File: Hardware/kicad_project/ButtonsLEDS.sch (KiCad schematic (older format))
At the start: 100 parts

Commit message: update project with corrected schematic / pcb
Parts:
- removed C? (x25): 1u, RandomJunk:C_0402_NoSilk, symbol Device:C
- removed D? (x25): D, RandomJunk:D_SOD-323F_less_silk, symbol Device:D
- removed D? (x25): WS2812B, RandomJunk:ws2812b-2020-lightpipe, symbol customLibrary:WS2812B-2020
- removed SW? (x25): spst_4_pin_internal, RandomJunk:ts1102_smallerpads_buttonhole, symbol customLibrary:spst_4_pin_internal
- added C10, C11, C12, C13, C14, C15, C16, C17, C18, C19, C20, C21, C22, C23, C24, C25, C6, C7, C8, C9: 1u, Capacitors_SMD:C_0402_NoSilk, symbol Device:C
- added D10, D11, D12, D13, D14, D15, D16, D17, D18, D19, D20, D21, D22, D23, D24, D25, D6, D7, D8, D9: WS2812B, RandomJunk:ws2812b-2020-lightpipe, symbol customLibrary:WS2812B-2020
- added D26, D27, D28, D29, D30, D31, D32, D33, D34, D35, D36, D37, D38, D39, D40, D41, D42, D43, D44, D45, D46, D47, D48, D49, D50: D, RandomJunk:D_SOD-323F_less_silk, symbol Device:D
- added SW1, SW10, SW11, SW12, SW13, SW14, SW15, SW16, SW17, SW18, SW19, SW2, SW20, SW21, SW22, SW23, SW24, SW25, SW3, SW4, SW5, SW6, SW7, SW8, SW9: spst_4_pin_internal, RandomJunk:ts1102_smallerpads_buttonhole, symbol customLibrary:spst_4_pin_internal
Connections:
- net +3V3: now also C10.1, C11.1, C12.1, C13.1, C14.1, C15.1, C16.1, C17.1, C18.1, C19.1, C20.1, C21.1, C22.1, C23.1, C24.1, C25.1, C6.1, C7.1, C8.1, C9.1, D10.4 (VDD), D11.4 (VDD), D12.4 (VDD), D13.4 (VDD), D14.4 (VDD), D15.4 (VDD), D16.4 (VDD), D17.4 (VDD), D18.4 (VDD), D19.4 (VDD), D20.4 (VDD), D21.4 (VDD), D22.4 (VDD), D23.4 (VDD), D24.4 (VDD), D25.4 (VDD), D6.4 (VDD), D7.4 (VDD), D8.4 (VDD), D9.4 (VDD)
- net GND: now also C10.2, C11.2, C12.2, C13.2, C14.2, C15.2, C16.2, C17.2, C18.2, C19.2, C20.2, C21.2, C22.2, C23.2, C24.2, C25.2, C6.2, C7.2, C8.2, C9.2, D10.2 (VSS), D11.2 (VSS), D12.2 (VSS), D13.2 (VSS), D14.2 (VSS), D15.2 (VSS), D16.2 (VSS), D17.2 (VSS), D18.2 (VSS), D19.2 (VSS), D20.2 (VSS), D21.2 (VSS), D22.2 (VSS), D23.2 (VSS), D24.2 (VSS), D25.2 (VSS), D6.2 (VSS), D7.2 (VSS), D8.2 (VSS), D9.2 (VSS)
- net key_col1: now also SW1.4
- net key_col2: now also SW2.4
- net key_col3: now also SW3.4
- net key_col4: now also SW4.4
- net key_col5: now also SW5.4
- net key_row1: now also D26.1 (K), D27.1 (K), D28.1 (K), D29.1 (K), D30.1 (K)
- net key_row2: now also D31.1 (K), D32.1 (K), D33.1 (K), D34.1 (K), D35.1 (K)
- net key_row3: now also D36.1 (K), D37.1 (K), D38.1 (K), D39.1 (K), D40.1 (K)
- net key_row4: now also D41.1 (K), D42.1 (K), D43.1 (K), D44.1 (K), D45.1 (K)
- net key_row5: now also D46.1 (K), D47.1 (K), D48.1 (K), D49.1 (K), D50.1 (K)
- net led_din: now also D6.3 (DIN)
- new net: D50.2 (A), SW25.1
- new net: SW20.3, SW25.4
- new net: D49.2 (A), SW24.1
- new net: SW19.3, SW24.4
- new net: D48.2 (A), SW23.1
- new net: SW18.3, SW23.4
- new net: D47.2 (A), SW22.1
- new net: SW17.3, SW22.4
- new net: D46.2 (A), SW21.1
- new net: SW16.3, SW21.4
- new net: D45.2 (A), SW20.1
- new net: SW15.3, SW20.4
- new net: D44.2 (A), SW19.1
- new net: SW14.3, SW19.4
- new net: D43.2 (A), SW18.1
- new net: SW13.3, SW18.4
- new net: D42.2 (A), SW17.1
- new net: SW12.3, SW17.4
- new net: D41.2 (A), SW16.1
- new net: SW11.3, SW16.4
- new net: D40.2 (A), SW15.1
- new net: SW10.3, SW15.4
- new net: D39.2 (A), SW14.1
- new net: SW14.4, SW9.3
- new net: D38.2 (A), SW13.1
- new net: SW13.4, SW8.3
- new net: D37.2 (A), SW12.1
- new net: SW12.4, SW7.3
- new net: D36.2 (A), SW11.1
- new net: SW11.4, SW6.3
- new net: D35.2 (A), SW10.1
- new net: SW10.4, SW5.3
- new net: D34.2 (A), SW9.1
- new net: SW4.3, SW9.4
- new net: D33.2 (A), SW8.1
- new net: SW3.3, SW8.4
- new net: D32.2 (A), SW7.1
- new net: SW2.3, SW7.4
- new net: D31.2 (A), SW6.1
- new net: SW1.3, SW6.4
- new net: D30.2 (A), SW5.1
- new net: D29.2 (A), SW4.1
- new net: D28.2 (A), SW3.1
- new net: D27.2 (A), SW2.1
- new net: D26.2 (A), SW1.1
- new net: D24.1 (DOUT), D25.3 (DIN)
- new net: D23.1 (DOUT), D24.3 (DIN)
- new net: D22.1 (DOUT), D23.3 (DIN)
- new net: D21.1 (DOUT), D22.3 (DIN)
- new net: D20.1 (DOUT), D21.3 (DIN)
- new net: D19.1 (DOUT), D20.3 (DIN)
- new net: D18.1 (DOUT), D19.3 (DIN)
- new net: D17.1 (DOUT), D18.3 (DIN)
- new net: D16.1 (DOUT), D17.3 (DIN)
- new net: D15.1 (DOUT), D16.3 (DIN)
- new net: D14.1 (DOUT), D15.3 (DIN)
- new net: D13.1 (DOUT), D14.3 (DIN)
- new net: D12.1 (DOUT), D13.3 (DIN)
- new net: D11.1 (DOUT), D12.3 (DIN)
- new net: D10.1 (DOUT), D11.3 (DIN)
- new net: D10.3 (DIN), D9.1 (DOUT)
- new net: D8.1 (DOUT), D9.3 (DIN)
- new net: D7.1 (DOUT), D8.3 (DIN)
- new net: D6.1 (DOUT), D7.3 (DIN)

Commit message: initial firmware commit, update hardware
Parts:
- D10, D11, D12, D13, D14, D15, D16, D17, D18, D19, D20, D21, D22, D23, D24, D25, D6, D7, D8, D9: LCSC C965555 -> C965556
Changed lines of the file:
@@
 F 2 "RandomJunk:ws2812b-2020-lightpipe" H 5150 5300 50  0001 L TNN
 F 3 "https://cdn-shop.adafruit.com/datasheets/WS2812B.pdf" H 5200 5225 50  0001 L TNN
-F 4 "C965555" H 5100 5600 50  0001 C CNN "LCSC"
+F 4 "C965556" H 5100 5600 50  0001 C CNN "LCSC"
 	1    5100 5600
 	1    0    0    -1
@@
 F 2 "RandomJunk:ws2812b-2020-lightpipe" H 4350 5300 50  0001 L TNN
 F 3 "https://cdn-shop.adafruit.com/datasheets/WS2812B.pdf" H 4400 5225 50  0001 L TNN
-F 4 "C965555" H 4300 5600 50  0001 C CNN "LCSC"
+F 4 "C965556" H 4300 5600 50  0001 C CNN "LCSC"
 	1    4300 5600
 	1    0    0    -1
@@
 F 2 "RandomJunk:ws2812b-2020-lightpipe" H 3550 5300 50  0001 L TNN
 F 3 "https://cdn-shop.adafruit.com/datasheets/WS2812B.pdf" H 3600 5225 50  0001 L TNN
-F 4 "C965555" H 3500 5600 50  0001 C CNN "LCSC"
+F 4 "C965556" H 3500 5600 50  0001 C CNN "LCSC"
 	1    3500 5600
 	1    0    0    -1
@@
 F 2 "RandomJunk:ws2812b-2020-lightpipe" H 2750 5300 50  0001 L TNN
 F 3 "https://cdn-shop.adafruit.com/datasheets/WS2812B.pdf" H 2800 5225 50  0001 L TNN
-F 4 "C965555" H 2700 5600 50  0001 C CNN "LCSC"
+F 4 "C965556" H 2700 5600 50  0001 C CNN "LCSC"
 	1    2700 5600
 	1    0    0    -1
@@
 F 2 "RandomJunk:ws2812b-2020-lightpipe" H 1950 5300 50  0001 L TNN
 F 3 "https://cdn-shop.adafruit.com/datasheets/WS2812B.pdf" H 2000 5225 50  0001 L TNN
-F 4 "C965555" H 1900 5600 50  0001 C CNN "LCSC"
+F 4 "C965556" H 1900 5600 50  0001 C CNN "LCSC"
 	1    1900 5600
 	1    0    0    -1
@@
 F 2 "RandomJunk:ws2812b-2020-lightpipe" H 5150 4350 50  0001 L TNN
 F 3 "https://cdn-shop.adafruit.com/datasheets/WS2812B.pdf" H 5200 4275 50  0001 L TNN
-F 4 "C965555" H 5100 4650 50  0001 C CNN "LCSC"
+F 4 "C965556" H 5100 4650 50  0001 C CNN "LCSC"
 	1    5100 4650
 	1    0    0    -1
@@
 F 2 "RandomJunk:ws2812b-2020-lightpipe" H 4350 4350 50  0001 L TNN
 F 3 "https://cdn-shop.adafruit.com/datasheets/WS2812B.pdf" H 4400 4275 50  0001 L TNN
-F 4 "C965555" H 4300 4650 50  0001 C CNN "LCSC"
+F 4 "C965556" H 4300 4650 50  0001 C CNN "LCSC"
 	1    4300 4650
 	1    0    0    -1
@@
 F 2 "RandomJunk:ws2812b-2020-lightpipe" H 3550 4350 50  0001 L TNN
 F 3 "https://cdn-shop.adafruit.com/datasheets/WS2812B.pdf" H 3600 4275 50  0001 L TNN
-F 4 "C965555" H 3500 4650 50  0001 C CNN "LCSC"
+F 4 "C965556" H 3500 4650 50  0001 C CNN "LCSC"
 	1    3500 4650
 	1    0    0    -1
@@
 F 2 "RandomJunk:ws2812b-2020-lightpipe" H 2750 4350 50  0001 L TNN
 F 3 "https://cdn-shop.adafruit.com/datasheets/WS2812B.pdf" H 2800 4275 50  0001 L TNN
-F 4 "C965555" H 2700 4650 50  0001 C CNN "LCSC"
+F 4 "C965556" H 2700 4650 50  0001 C CNN "LCSC"
 	1    2700 4650
 	1    0    0    -1
@@
 F 2 "RandomJunk:ws2812b-2020-lightpipe" H 1950 4350 50  0001 L TNN
 F 3 "https://cdn-shop.adafruit.com/datasheets/WS2812B.pdf" H 2000 4275 50  0001 L TNN
-F 4 "C965555" H 1900 4650 50  0001 C CNN "LCSC"
+F 4 "C965556" H 1900 4650 50  0001 C CNN "LCSC"
 	1    1900 4650
 	1    0    0    -1
@@
 F 2 "RandomJunk:ws2812b-2020-lightpipe" H 5150 3400 50  0001 L TNN
 F 3 "https://cdn-shop.adafruit.com/datasheets/WS2812B.pdf" H 5200 3325 50  0001 L TNN
-F 4 "C965555" H 5100 3700 50  0001 C CNN "LCSC"
+F 4 "C965556" H 5100 3700 50  0001 C CNN "LCSC"
 	1    5100 3700
 	1    0    0    -1
@@
 F 2 "RandomJunk:ws2812b-2020-lightpipe" H 4350 3400 50  0001 L TNN
 F 3 "https://cdn-shop.adafruit.com/datasheets/WS2812B.pdf" H 4400 3325 50  0001 L TNN
-F 4 "C965555" H 4300 3700 50  0001 C CNN "LCSC"
+F 4 "C965556" H 4300 3700 50  0001 C CNN "LCSC"
 	1    4300 3700
 	1    0    0    -1
@@
 F 2 "RandomJunk:ws2812b-2020-lightpipe" H 3550 3400 50  0001 L TNN
 F 3 "https://cdn-shop.adafruit.com/datasheets/WS2812B.pdf" H 3600 3325 50  0001 L TNN
-F 4 "C965555" H 3500 3700 50  0001 C CNN "LCSC"
+F 4 "C965556" H 3500 3700 50  0001 C CNN "LCSC"
 	1    3500 3700
 	1    0    0    -1
@@
 F 2 "RandomJunk:ws2812b-2020-lightpipe" H 2750 3400 50  0001 L TNN
 F 3 "https://cdn-shop.adafruit.com/datasheets/WS2812B.pdf" H 2800 3325 50  0001 L TNN
-F 4 "C965555" H 2700 3700 50  0001 C CNN "LCSC"
+F 4 "C965556" H 2700 3700 50  0001 C CNN "LCSC"
 	1    2700 3700
 	1    0    0    -1
@@
 F 2 "RandomJunk:ws2812b-2020-lightpipe" H 1950 3400 50  0001 L TNN
 F 3 "https://cdn-shop.adafruit.com/datasheets/WS2812B.pdf" H 2000 3325 50  0001 L TNN
-F 4 "C965555" H 1900 3700 50  0001 C CNN "LCSC"
+F 4 "C965556" H 1900 3700 50  0001 C CNN "LCSC"
 	1    1900 3700
 	1    0    0    -1
@@
 F 2 "RandomJunk:ws2812b-2020-lightpipe" H 5150 2450 50  0001 L TNN
 F 3 "https://cdn-shop.adafruit.com/datasheets/WS2812B.pdf" H 5200 2375 50  0001 L TNN
-F 4 "C965555" H 5100 2750 50  0001 C CNN "LCSC"
+F 4 "C965556" H 5100 2750 50  0001 C CNN "LCSC"
 	1    5100 2750
 	1    0    0    -1
@@
 F 2 "RandomJunk:ws2812b-2020-lightpipe" H 4350 2450 50  0001 L TNN
 F 3 "https://cdn-shop.adafruit.com/datasheets/WS2812B.pdf" H 4400 2375 50  0001 L TNN
-F 4 "C965555" H 4300 2750 50  0001 C CNN "LCSC"
+F 4 "C965556" H 4300 2750 50  0001 C CNN "LCSC"
 	1    4300 2750
 	1    0    0    -1
@@
 F 2 "RandomJunk:ws2812b-2020-lightpipe" H 3550 2450 50  0001 L TNN
 F 3 "https://cdn-shop.adafruit.com/datasheets/WS2812B.pdf" H 3600 2375 50  0001 L TNN
-F 4 "C965555" H 3500 2750 50  0001 C CNN "LCSC"
+F 4 "C965556" H 3500 2750 50  0001 C CNN "LCSC"
 	1    3500 2750
 	1    0    0    -1
@@
 F 2 "RandomJunk:ws2812b-2020-lightpipe" H 2750 2450 50  0001 L TNN
 F 3 "https://cdn-shop.adafruit.com/datasheets/WS2812B.pdf" H 2800 2375 50  0001 L TNN
-F 4 "C965555" H 2700 2750 50  0001 C CNN "LCSC"
+F 4 "C965556" H 2700 2750 50  0001 C CNN "LCSC"
 	1    2700 2750
 	1    0    0    -1
@@
 F 2 "RandomJunk:ws2812b-2020-lightpipe" H 1950 2450 50  0001 L TNN
 F 3 "https://cdn-shop.adafruit.com/datasheets/WS2812B.pdf" H 2000 2375 50  0001 L TNN
-F 4 "C965555" H 1900 2750 50  0001 C CNN "LCSC"
+F 4 "C965556" H 1900 2750 50  0001 C CNN "LCSC"
 	1    1900 2750
 	1    0    0    -1

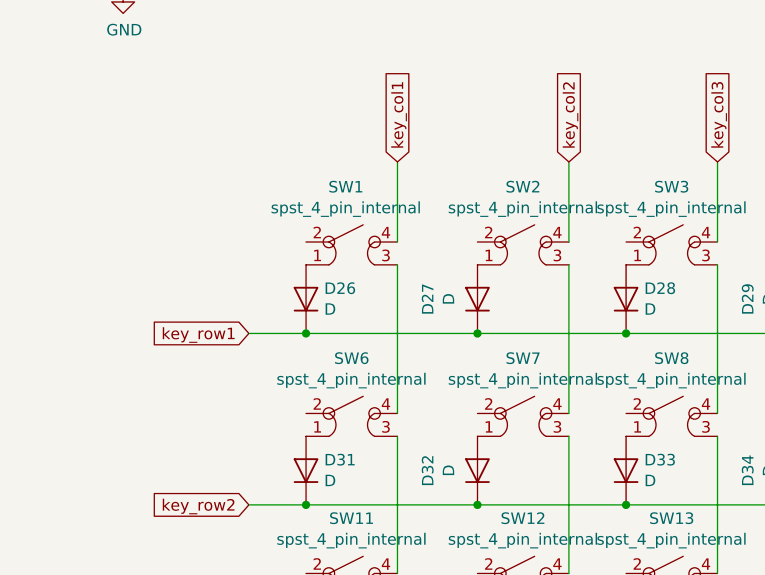
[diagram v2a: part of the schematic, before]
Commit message: new hardware rev
- soft / latching power switch
- corrected mic
- added pullup to flash ss
- front & back enclosure plates
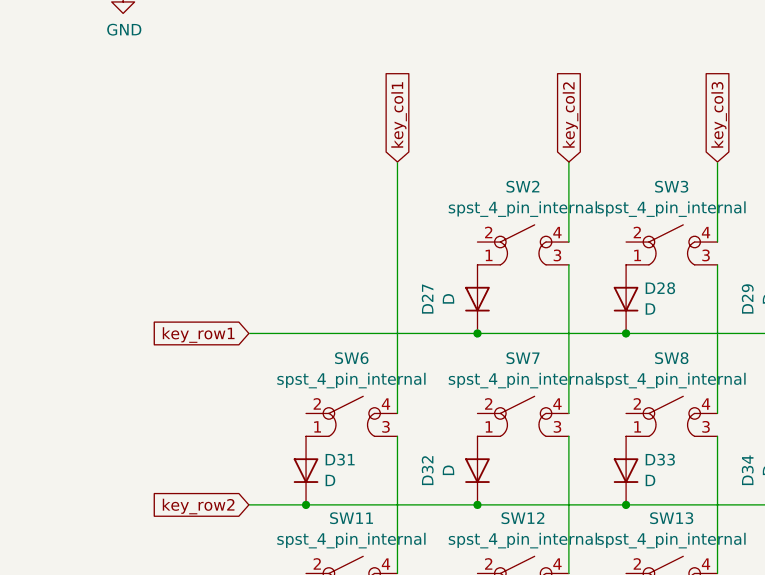
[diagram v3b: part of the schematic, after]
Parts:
- removed D26: D, RandomJunk:D_SOD-323F_less_silk, symbol Device:D
- removed SW1: spst_4_pin_internal, RandomJunk:ts1102_smallerpads_buttonhole, symbol customLibrary:spst_4_pin_internal
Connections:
- net key_col1: now also SW6.4
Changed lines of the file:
@@
 Wire Wire Line
 	3100 7300 3100 7950
-Wire Wire Line
-	2350 7300 2350 7950
 $Comp
 L customLibrary:spst_4_pin_internal SW?
@@
 Text GLabel 1700 7600 0    50   Input ~ 0
 key_row1
-Wire Wire Line
-	2350 6850 2350 7200
-$Comp
-L customLibrary:spst_4_pin_internal SW?
-U 1 1 617D2BA0
-P 2150 7350
-AR Path="/617D2BA0" Ref="SW?"  Part="1"
-AR Path="/631EE57A/617D2BA0" Ref="SW1"  Part="1"
-F 0 "SW1" H 2125 7740 50  0000 C CNN
-F 1 "spst_4_pin_internal" H 2125 7649 50  0000 C CNN
-F 2 "RandomJunk:ts1102_smallerpads_buttonhole" H 2150 7350 50  0001 C CNN
-F 3 "" H 2150 7350 50  0001 C CNN
-F 4 "C480275" H 2150 7350 50  0001 C CNN "LCSC"
-	1    2150 7350
-	1    0    0    -1
-$EndComp
 Wire Wire Line
 	5550 5450 5550 5300
@@
 $EndComp
 Wire Wire Line
-	1950 7600 1700 7600
-Wire Wire Line
-	2700 7600 1950 7600
-Connection ~ 1950 7600
-$Comp
-L Device:D D?
-U 1 1 617D2F04
-P 1950 7450
-AR Path="/617D2F04" Ref="D?"  Part="1"
-AR Path="/631EE57A/617D2F04" Ref="D26"  Part="1"
-F 0 "D26" V 1996 7371 50  0000 R CNN
-F 1 "D" V 1905 7371 50  0000 R CNN
-F 2 "RandomJunk:D_SOD-323F_less_silk" H 1950 7450 50  0001 C CNN
-F 3 "~" H 1950 7450 50  0001 C CNN
-F 4 "c2128" H 1950 7450 50  0001 C CNN "LCSC"
-	1    1950 7450
-	0    -1   -1   0
-$EndComp
-Wire Wire Line
 	1150 2750 1600 2750
 $Comp
@@
 $EndComp
 Connection ~ 5900 2450
+Wire Wire Line
+	1700 7600 2700 7600
+Wire Wire Line
+	2350 6850 2350 7950
 $EndSCHEMATC
